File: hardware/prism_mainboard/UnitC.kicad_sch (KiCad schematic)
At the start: 1 part, among them U1 XC7Z010-1CLG400C

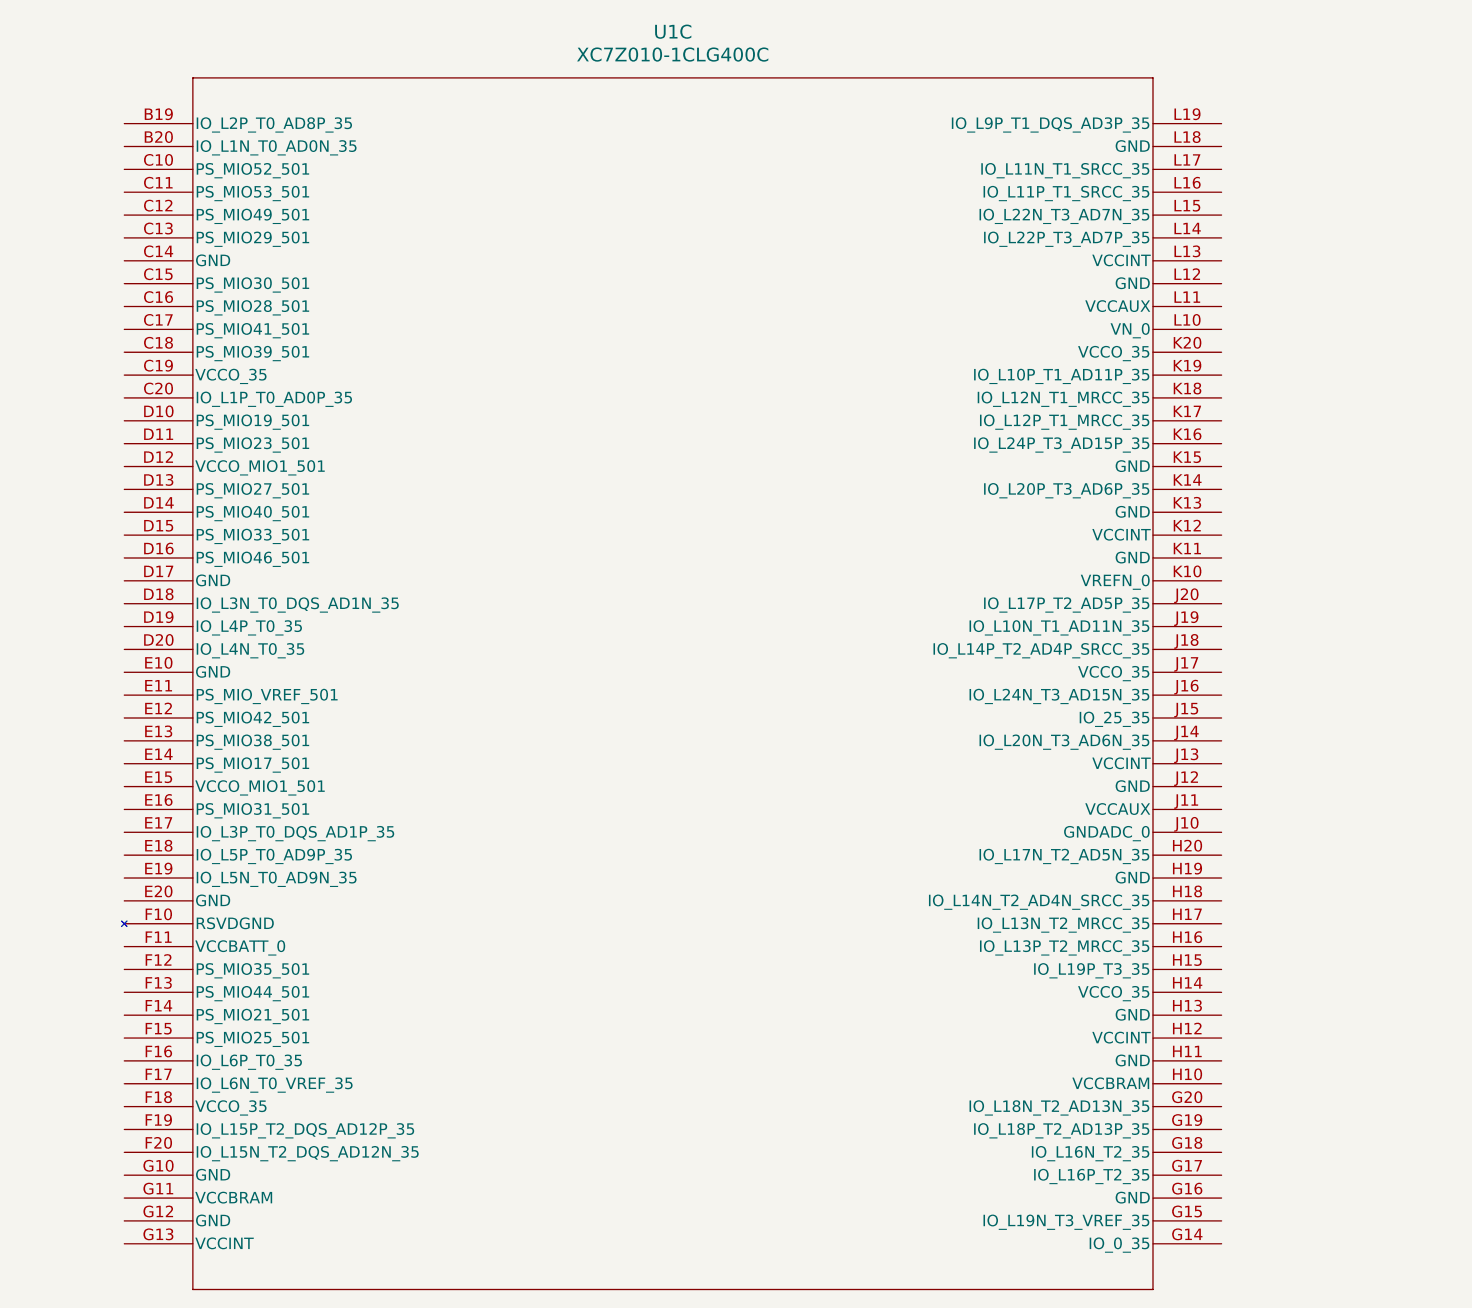
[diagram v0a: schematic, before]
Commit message: Zynq-7000 Schematic Updates
Added basic power net labels for the PL and PS portions of the FPGA.
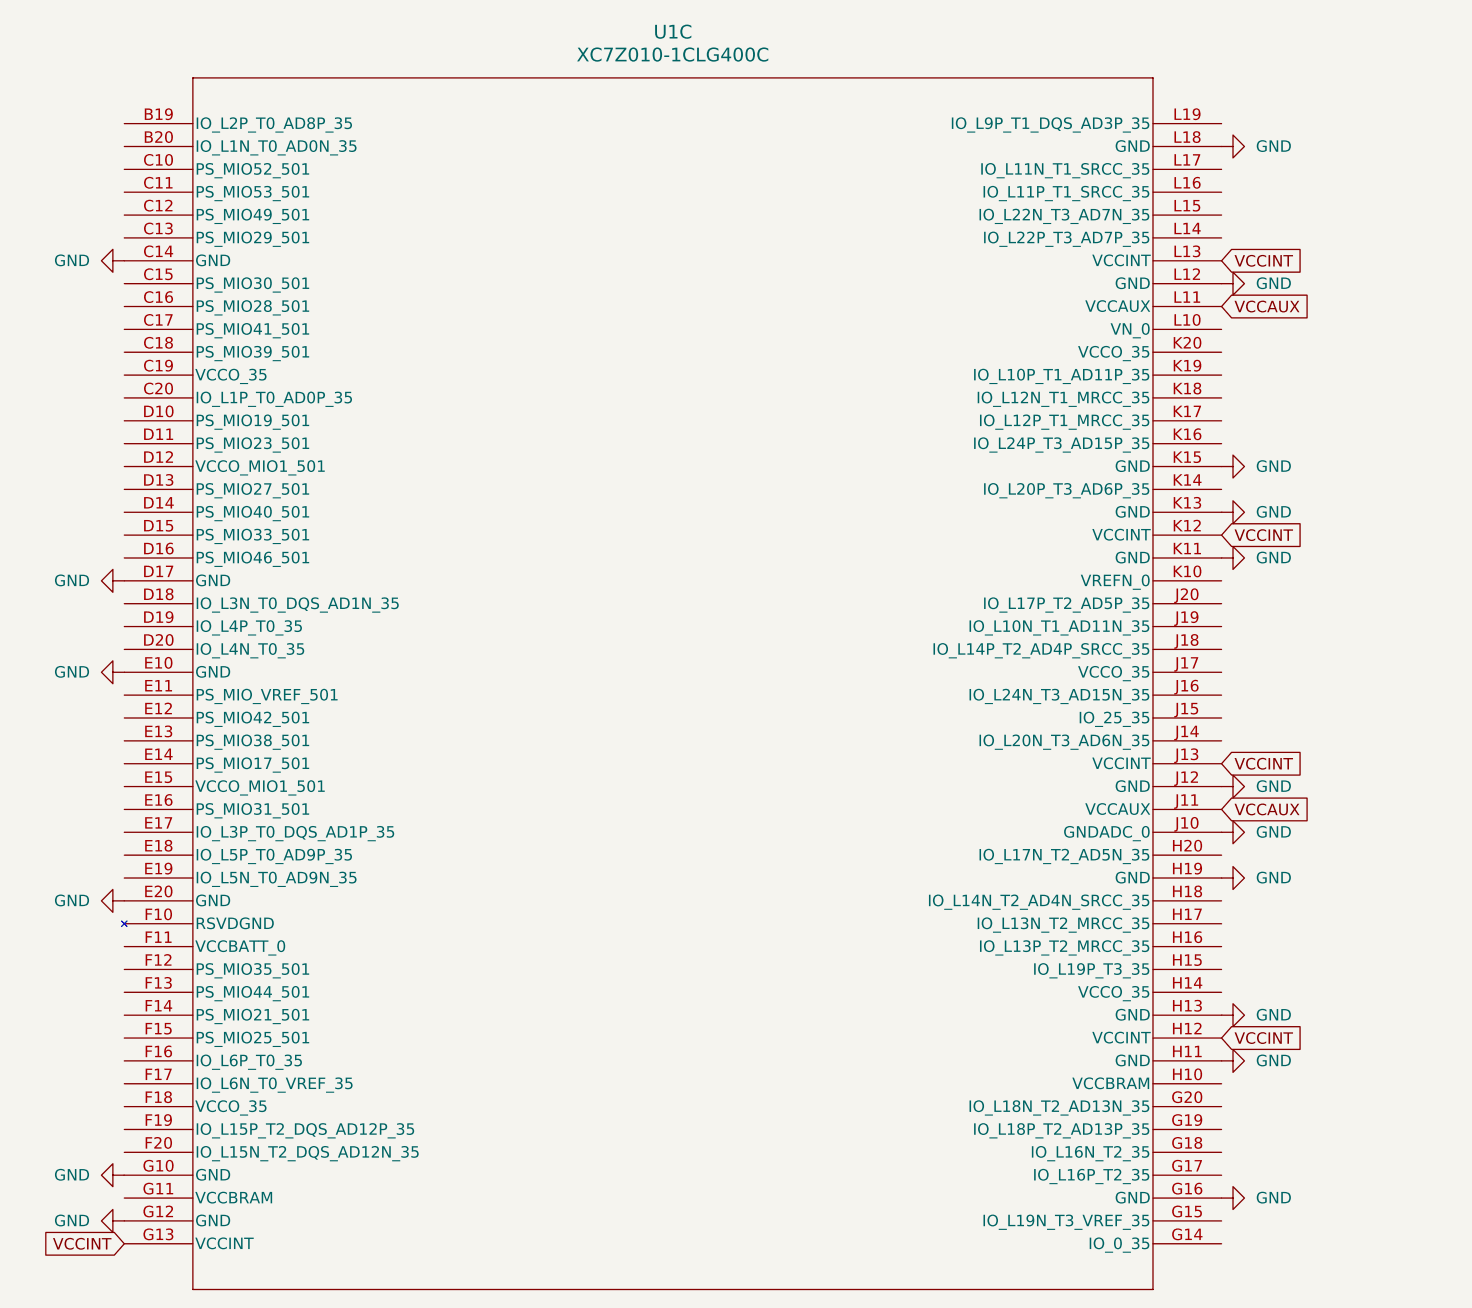
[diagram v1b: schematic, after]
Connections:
- net GND: now reaches U1.C14 (GND)
- net GND: now also U1.D17 (GND), U1.E10 (GND), U1.E20 (GND), U1.G10 (GND), U1.G12 (GND), U1.G16 (GND), U1.H11 (GND), U1.H13 (GND), U1.H19 (GND), U1.J10 (GNDADC_0), U1.J12 (GND), U1.K11 (GND), U1.K13 (GND), U1.K15 (GND), U1.L12 (GND), U1.L18 (GND)
- net VCCINT: now reaches U1.G13 (VCCINT)
- net VCCINT: now also U1.H12 (VCCINT), U1.J13 (VCCINT), U1.K12 (VCCINT), U1.L13 (VCCINT)
- net VCCAUX: now reaches U1.J11 (VCCAUX)
- net VCCAUX: now also U1.L11 (VCCAUX)

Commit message: Mainboard Updates
Started a lot of the basic schematic nets like GND and Power nets. Major Change: Decided on using the XC7Z015-1CLG485I instead of the 7010 or 7020 due to the ability to use HDMI interfaces with an adapter and more LUTs. Updated schematic symbols and footprints accordingly. Added Memory, Encoder, MicroSD schematics. Added LimeSDR footprints as well. Will Try to add Power to the entire board next.
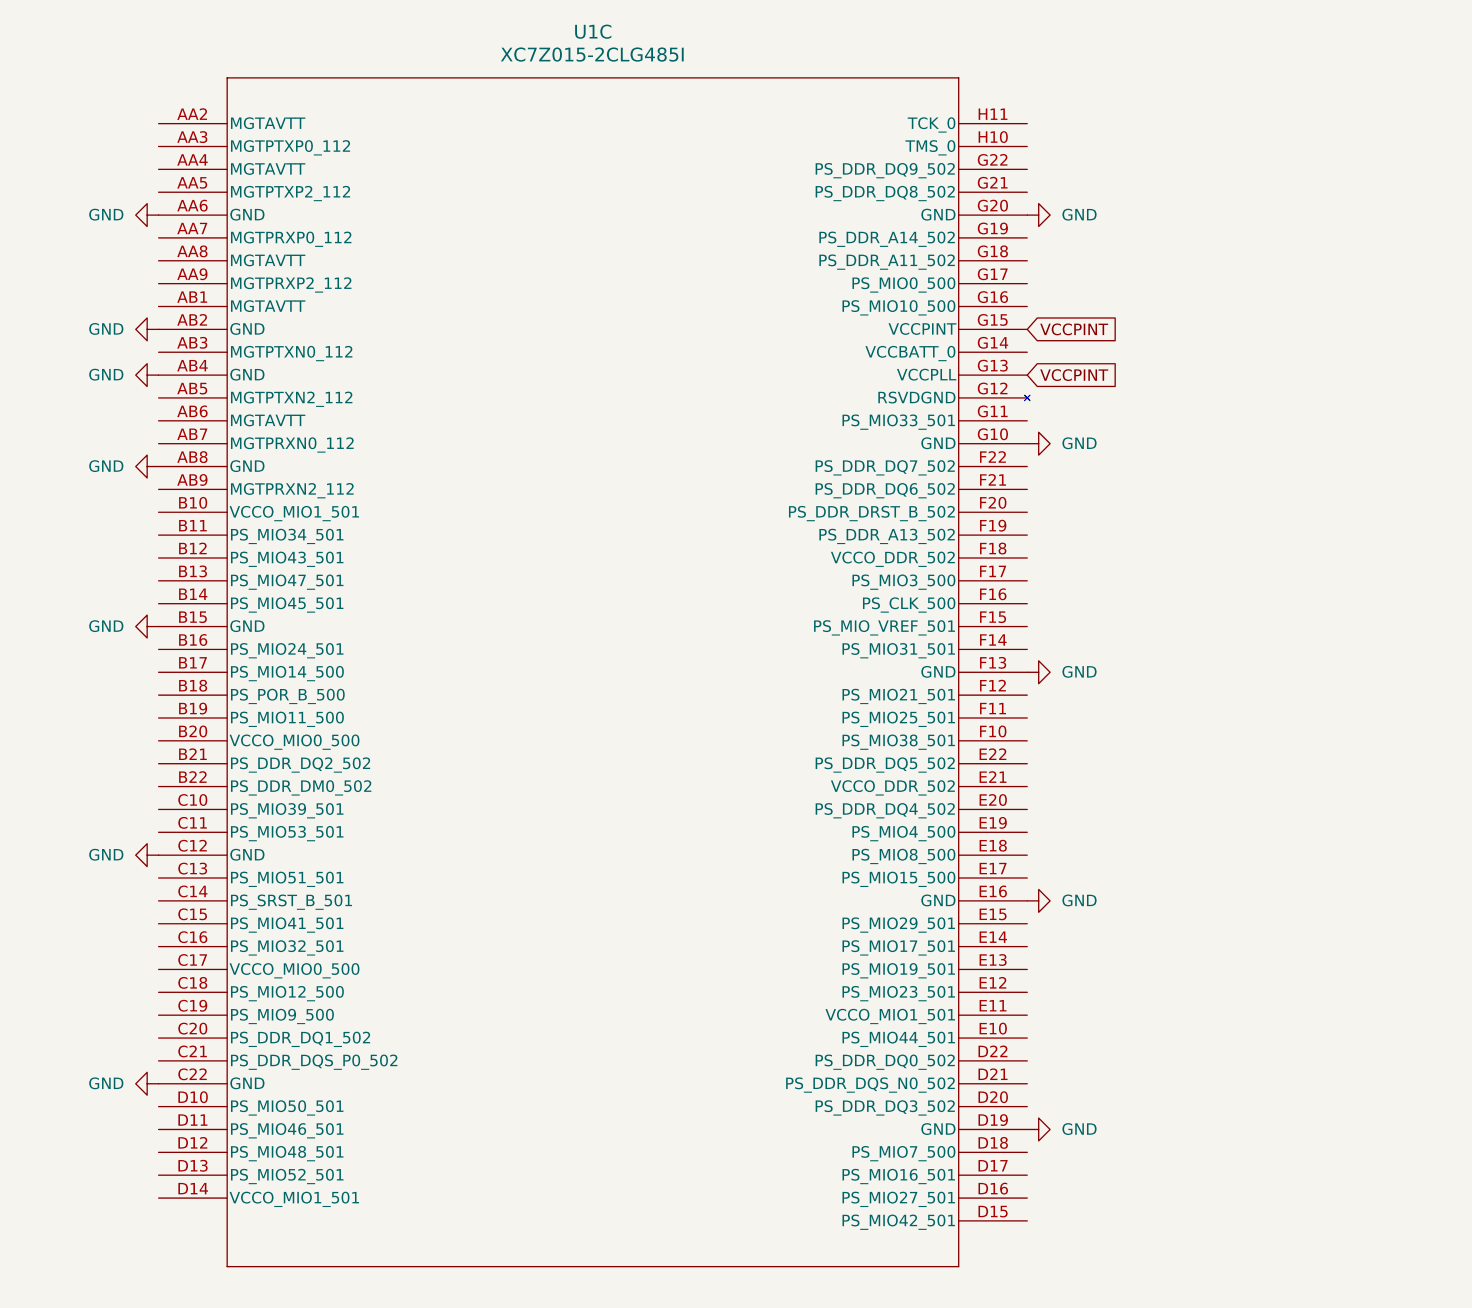
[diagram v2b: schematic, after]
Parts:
- removed U1: XC7Z010-1CLG400C, XC7Z010-1CLG400C:CLG400_XIL, symbol XC7Z010-1CLG400C:XC7Z010-1CLG400C
- added U1: XC7Z015-2CLG485I, CLG485_XIL, symbol XC7Z015-CLG485:XC7Z015-2CLG485I
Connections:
- net GND: now also U1.AA6 (GND), U1.AB2 (GND), U1.AB4 (GND), U1.AB8 (GND), U1.B15 (GND), U1.C12 (GND), U1.C22 (GND), U1.D19 (GND), U1.E16 (GND), U1.F13 (GND), U1.G10 (GND), U1.G20 (GND)
- new net VCCPINT: U1.G13 (VCCPLL), U1.G15 (VCCPINT)

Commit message: Schematic Updates
Updated the DDR3 DRAM to 4Gb, added a lot of nets and started updating the power and decoupling components. Updated .gitignore to avoid .mkv files.
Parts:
- added R5, R6: 20k, symbol Device:R
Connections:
- net GND: now also R6.2
- net VCCO_MIO1: now reaches U1.B10 (VCCO_MIO1_501)
- net VCCO_MIO1: now also U1.D14 (VCCO_MIO1_501), U1.E11 (VCCO_MIO1_501)
- net VCCO_MIO0: now reaches U1.B20 (VCCO_MIO0_500)
- net VCCO_MIO0: now also U1.C17 (VCCO_MIO0_500), R5.2
- net at U1.D18 (PS_MIO7_500): now also R5.1
- net at U1.E18 (PS_MIO8_500): now also R6.1
- net VCCO_DDR: now reaches U1.E21 (VCCO_DDR_502)
- net VCCO_DDR: now also U1.F18 (VCCO_DDR_502)

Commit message: Updated PCB
Missing footprints due to not being properly loaded on this version, will update on other PC to consolidate layout. Will work on DDR3 lines to Zynq-7000 Processing System Next.
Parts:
- R5, R6: footprint (none) -> Capacitor_SMD:C_0805_2012Metric_Pad1.18x1.45mm_HandSolder
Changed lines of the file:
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@@
 			)
 		)
-		(property "Footprint" ""
+		(property "Footprint" "Capacitor_SMD:C_0805_2012Metric_Pad1.18x1.45mm_HandSolder"
 			(at 195.58 112.268 90)
 			(hide yes)
@@
 			)
 		)
-		(property "Footprint" ""
+		(property "Footprint" "Capacitor_SMD:C_0805_2012Metric_Pad1.18x1.45mm_HandSolder"
 			(at 198.12 145.288 90)
 			(hide yes)
